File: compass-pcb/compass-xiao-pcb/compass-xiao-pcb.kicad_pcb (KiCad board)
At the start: 2 copper layers, 25 parts

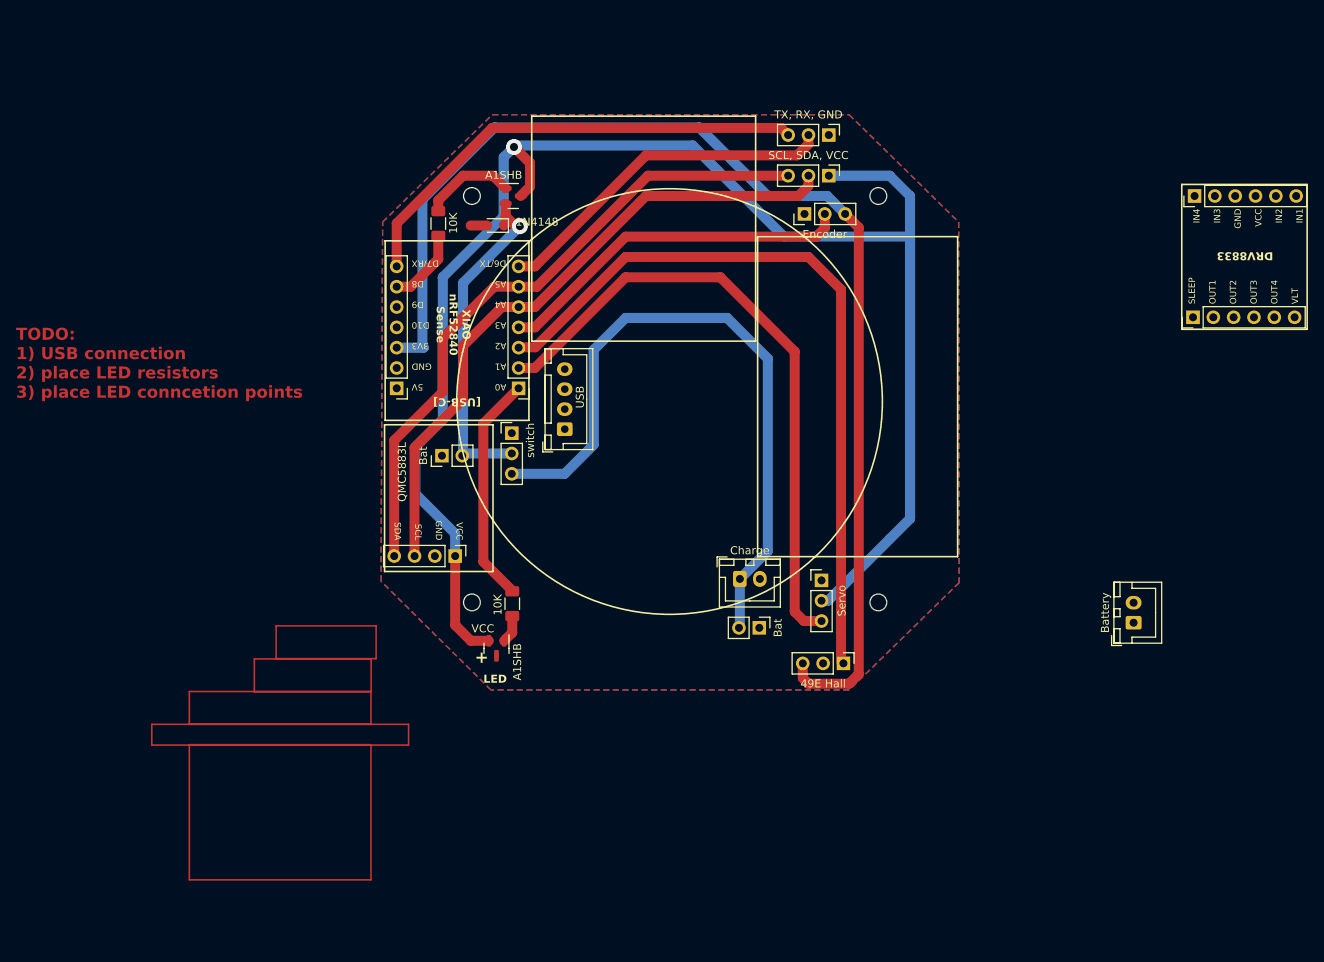
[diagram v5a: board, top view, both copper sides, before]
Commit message: added LED connection points
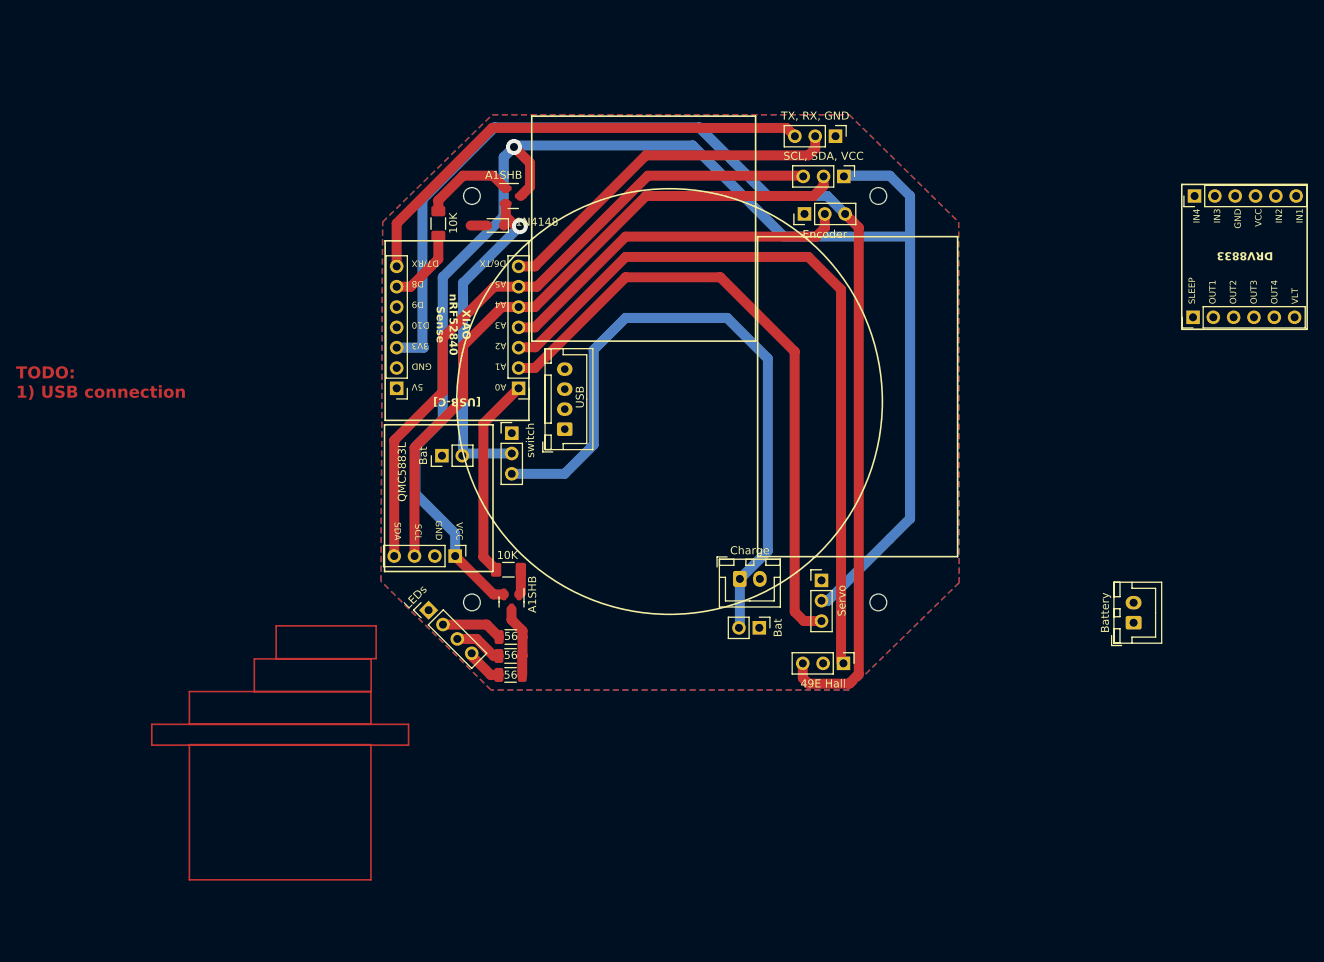
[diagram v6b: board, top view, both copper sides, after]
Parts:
- added 56: R_1206_3216Metric, Resistor_SMD:R_1206_3216Metric, F.Cu at (117.7, 118.5)
- added 56: R_1206_3216Metric, Resistor_SMD:R_1206_3216Metric, F.Cu at (117.7, 120.8)
- added 56: R_1206_3216Metric, Resistor_SMD:R_1206_3216Metric, F.Cu at (117.7, 116.1)
- added LEDs: PinHeader_1x04_P2.54mm_Vertical, Connector_PinHeader_2.54mm:PinHeader_1x04_P2.54mm_Vertical, F.Cu at (107.5, 112.7)
- moved A1SHB 6.09 mm to (117.8, 111.7)
- moved 10K 4.27 mm to (117.4, 107.7), turned to 180 degrees
- moved REF** 1.89 mm to (159.4, 58.5)
- moved REF** 0.85 mm to (158.3, 53.5)
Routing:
- net (no net): track 1052.1 -> 1073.7 mm
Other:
- board text added: "TODO: 1) USB connection"
- board text removed: "+"
- board text removed: "LED"
- board text removed: "TODO: 1) USB connection 2) place LED resistors 3) place LED conncetion points"
- board text removed: "VCC"

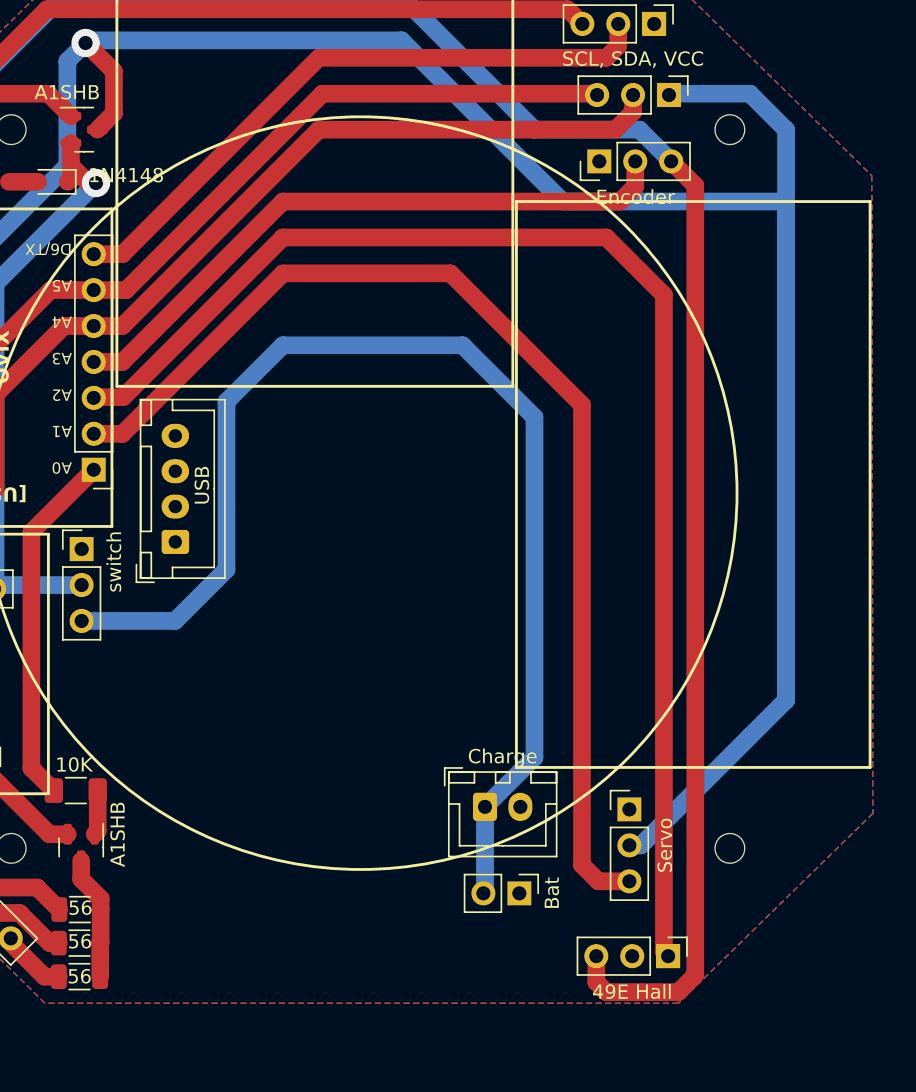
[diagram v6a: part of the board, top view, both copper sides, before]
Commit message: more room for servo connector
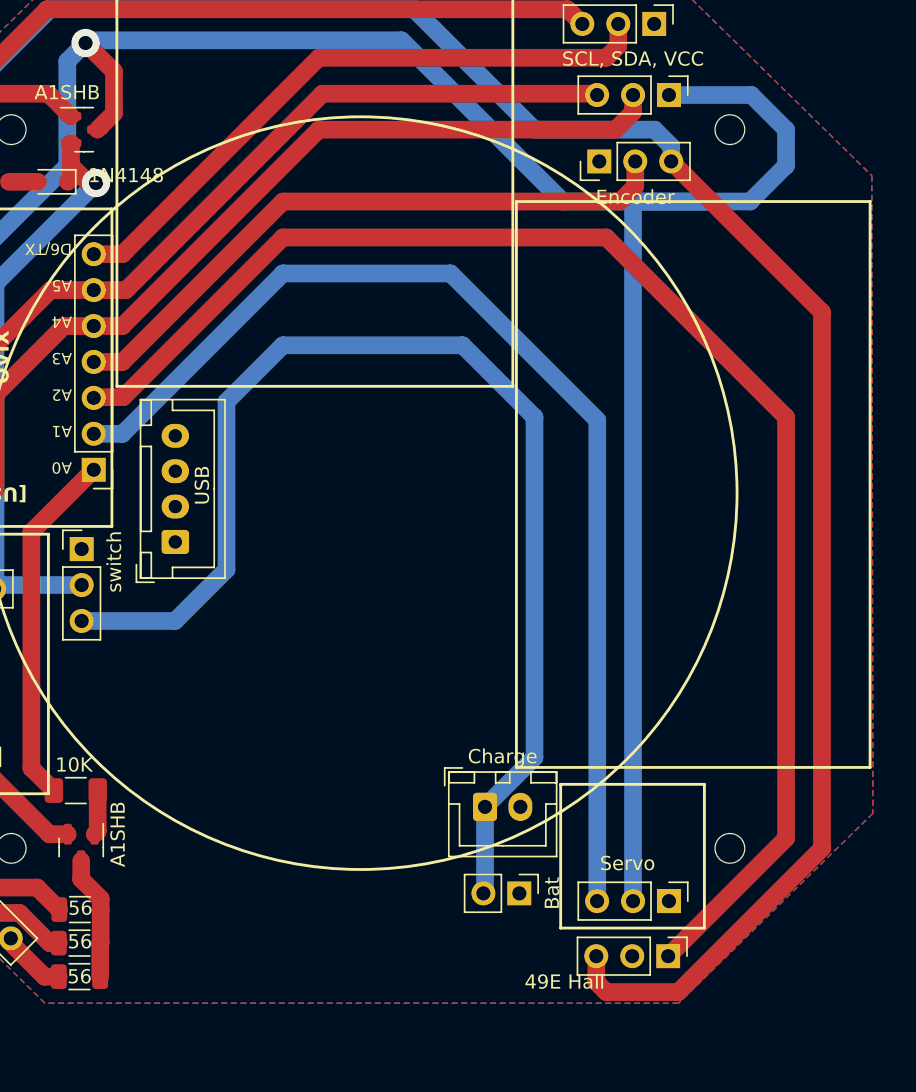
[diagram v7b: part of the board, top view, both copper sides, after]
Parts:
- moved Servo 7.06 mm to (159.4, 115.5), turned to -90 degrees
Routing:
- net (no net): track 1073.7 -> 1055.6 mm

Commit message: minor polishing
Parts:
- moved Servo 0.38 mm to (159.4, 115.1)
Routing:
- net (no net): track 1055.6 -> 1054.3 mm
